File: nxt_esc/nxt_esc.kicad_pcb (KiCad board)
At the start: 2 copper layers, 47.6 x 47.6 mm, 18 parts, among them IC1 L293D, J1 NXT_MOTOR, J2 NXT_MOTOR, SW1 Skid Steer/Drive & Steer, SW2 Center Steering, U1 LM7805CT

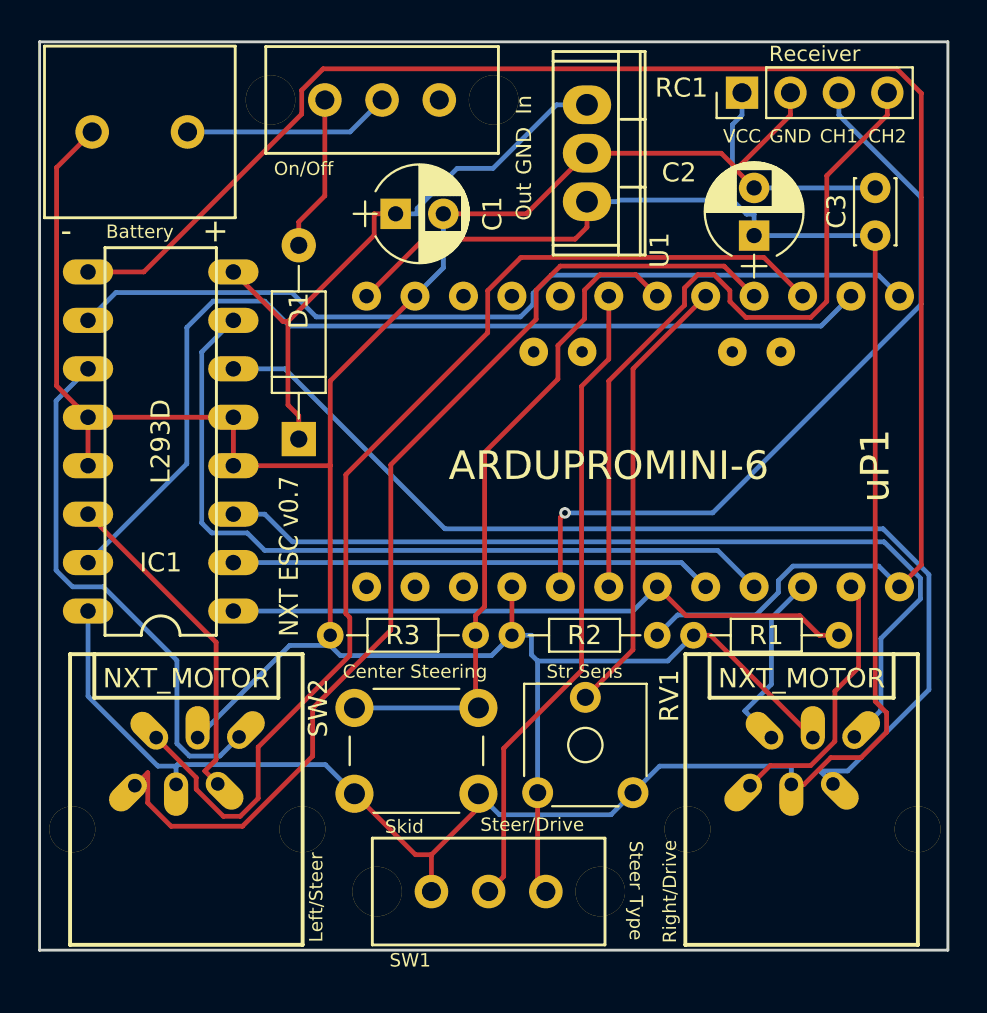
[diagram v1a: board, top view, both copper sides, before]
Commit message: Started adding wider traces
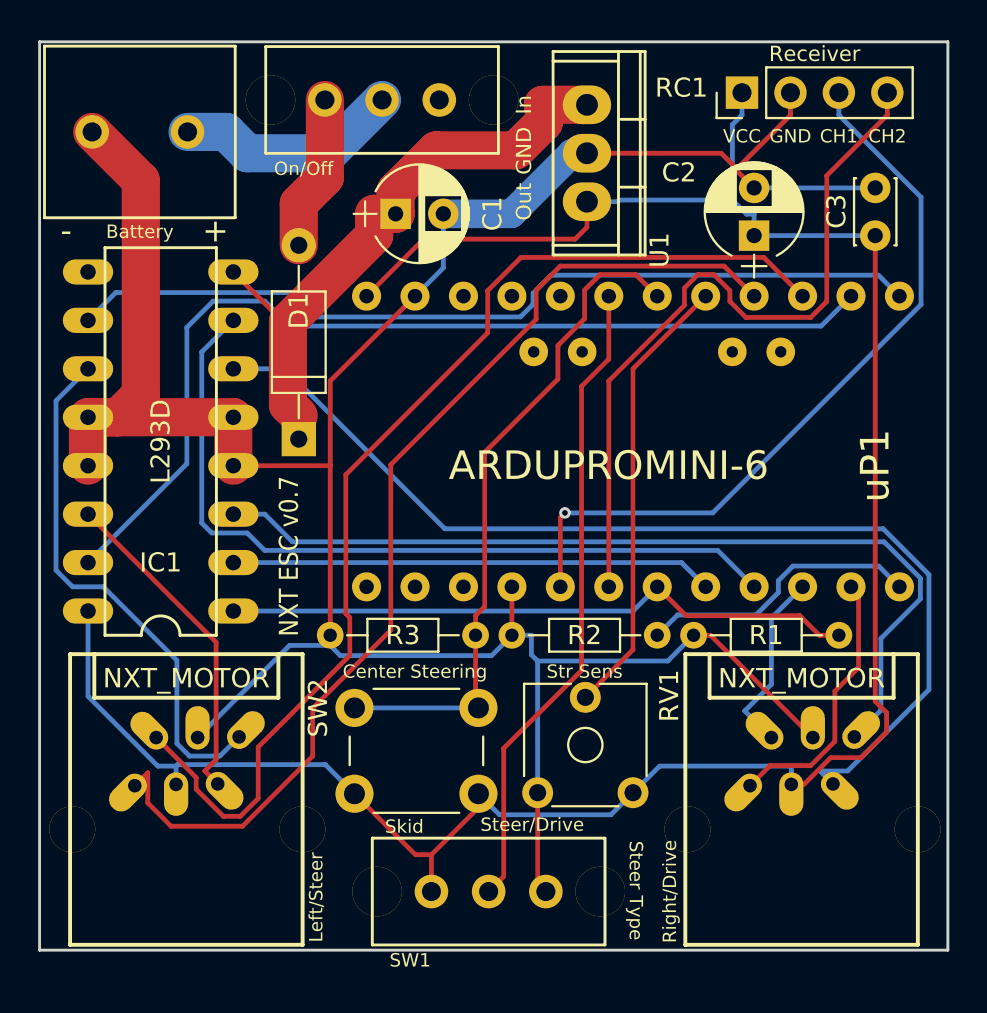
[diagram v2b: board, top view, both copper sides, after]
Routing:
- net Net-(IC1-Pad9): track 90.7 -> 15.0 mm
- net GND: track 142.9 -> 144.5 mm
- net VCC: track 31.5 -> 32.7 mm
- net Net-(BT1-Pad1): track 10.9 -> 11.8 mm
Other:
- net class H-Bridge Power added: clearance 0.2, trace_width 4, via_dia 4.5, via_drill 4.3
- net class Motor Power added: clearance 0.2, trace_width 1.5, via_dia 3, via_drill 2.8
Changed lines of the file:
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@@
   (general
     (links 57)
-    (no_connects 0)
-    (area 111.049999 65.73 176.91 125.170001)
+    (no_connects 1)
+    (area 111.049999 77.394999 158.825001 125.170001)
     (thickness 1.6)
     (drawings 24)
-    (tracks 254)
+    (tracks 251)
     (zones 0)
     (modules 18)
@@
   )
   (setup
-    (last_trace_width 0.25)
+    (last_trace_width 1.5)
     (user_trace_width 0.4)
+    (user_trace_width 0.75)
+    (user_trace_width 1.5)
     (trace_clearance 0.2)
     (zone_clearance 0.508)
@@
     (add_net "Net-(SW1-Pad2)")
     (add_net VCC)
+  )
+  (net_class "H-Bridge Power" ""
+    (clearance 0.2)
+    (trace_width 4)
+    (via_dia 4.5)
+    (via_drill 4.3)
+    (uvia_dia 2.3)
+    (uvia_drill 2)
+  )
+  (net_class "Motor Power" ""
+    (clearance 0.2)
+    (trace_width 1.5)
+    (via_dia 3)
+    (via_drill 2.8)
+    (uvia_dia 1.3)
+    (uvia_drill 0.8)
   )
   (module ArduProMiniTKB:ArduProMini-6 (layer F.Cu)
@@
   (segment (start 119.6273 93.7327) (end 119.6273 102.6983) (width 0.25) (layer B.Cu) (net 3))
   (segment (start 121.285 92.075) (end 119.6273 93.7327) (width 0.25) (layer B.Cu) (net 3))
-  (segment (start 139.827 80.772) (end 138.2317 80.772) (width 0.25) (layer B.Cu) (net 4))
-  (segment (start 129.794 86.487) (end 130.9193 86.487) (width 0.25) (layer B.Cu) (net 4))
-  (segment (start 134.8998 84.1039) (end 138.2317 80.772) (width 0.25) (layer B.Cu) (net 4))
-  (segment (start 133.021 84.1039) (end 134.8998 84.1039) (width 0.25) (layer B.Cu) (net 4))
-  (segment (start 130.9193 86.2056) (end 133.021 84.1039) (width 0.25) (layer B.Cu) (net 4))
-  (segment (start 130.9193 86.487) (end 130.9193 86.2056) (width 0.25) (layer B.Cu) (net 4))
+  (segment (start 139.827 80.772) (end 137.5156 80.772) (width 2) (layer F.Cu) (net 4) (status 400000))
+  (segment (start 129.794 85.2932) (end 129.794 86.487) (width 2) (layer F.Cu) (net 4) (status 800000))
+  (segment (start 131.9276 83.1596) (end 129.794 85.2932) (width 2) (layer F.Cu) (net 4))
+  (segment (start 136.0932 83.1596) (end 131.9276 83.1596) (width 2) (layer F.Cu) (net 4))
+  (segment (start 137.5664 81.6864) (end 136.0932 83.1596) (width 2) (layer F.Cu) (net 4))
+  (segment (start 137.5664 80.8228) (end 137.5664 81.6864) (width 2) (layer F.Cu) (net 4))
+  (segment (start 137.5156 80.772) (end 137.5664 80.8228) (width 2) (layer F.Cu) (net 4))
   (segment (start 123.883 92.133) (end 121.285 89.535) (width 0.25) (layer F.Cu) (net 4))
   (segment (start 124.148 92.133) (end 123.883 92.133) (width 0.25) (layer F.Cu) (net 4))
-  (segment (start 128.6687 87.6123) (end 124.148 92.133) (width 0.25) (layer F.Cu) (net 4))
-  (segment (start 128.6687 86.487) (end 128.6687 87.6123) (width 0.25) (layer F.Cu) (net 4))
-  (segment (start 124.148 96.5067) (end 124.714 97.0727) (width 0.25) (layer F.Cu) (net 4))
-  (segment (start 124.148 92.133) (end 124.148 96.5067) (width 0.25) (layer F.Cu) (net 4))
-  (segment (start 129.794 86.487) (end 128.6687 86.487) (width 0.25) (layer F.Cu) (net 4))
+  (segment (start 128.6687 87.6123) (end 124.148 92.133) (width 2) (layer F.Cu) (net 4))
+  (segment (start 128.6687 86.487) (end 128.6687 87.6123) (width 2) (layer F.Cu) (net 4))
+  (segment (start 124.148 96.5067) (end 124.714 97.0727) (width 2) (layer F.Cu) (net 4))
+  (segment (start 124.148 92.133) (end 124.148 96.5067) (width 2) (layer F.Cu) (net 4))
+  (segment (start 129.794 86.487) (end 128.6687 86.487) (width 2) (layer F.Cu) (net 4))
   (segment (start 124.714 98.298) (end 124.714 97.0727) (width 0.25) (layer F.Cu) (net 4))
   (segment (start 153.8425 113.9143) (end 155.24 112.5168) (width 0.25) (layer B.Cu) (net 5))
@@
   (segment (start 155.24 112.5168) (end 155.2399 112.5168) (width 0.25) (layer B.Cu) (net 5))
   (segment (start 121.285 102.235) (end 122.9311 102.235) (width 0.25) (layer B.Cu) (net 5))
+  (segment (start 132.294 86.487) (end 135.8646 86.487) (width 1.5) (layer B.Cu) (net 6) (status 400000))
+  (segment (start 135.8646 86.487) (end 139.0396 83.312) (width 1.5) (layer B.Cu) (net 6) (status 800000))
+  (segment (start 139.0396 83.312) (end 139.827 83.312) (width 1.5) (layer B.Cu) (net 6) (status C00000))
+  (segment (start 121.285 97.155) (end 121.285 99.695) (width 2) (layer F.Cu) (net 6))
+  (segment (start 113.665 97.155) (end 121.285 97.155) (width 2) (layer F.Cu) (net 6))
+  (segment (start 113.665 97.155) (end 113.665 99.695) (width 2) (layer F.Cu) (net 6))
+  (segment (start 113.665 97.155) (end 115.2398 97.155) (width 2) (layer F.Cu) (net 6))
+  (segment (start 116.4336 84.745) (end 113.883 82.1944) (width 2) (layer F.Cu) (net 6))
+  (segment (start 116.4336 95.9612) (end 116.4336 84.745) (width 2) (layer F.Cu) (net 6))
+  (segment (start 115.2398 97.155) (end 116.4336 95.9612) (width 2) (layer F.Cu) (net 6))
   (segment (start 154.94 85.13) (end 148.59 85.13) (width 0.25) (layer B.Cu) (net 6))
   (segment (start 135.89 108.585) (end 135.89 106.045) (width 0.25) (layer F.Cu) (net 6))
-  (segment (start 121.285 97.155) (end 121.285 99.695) (width 0.25) (layer F.Cu) (net 6))
-  (segment (start 113.665 97.155) (end 121.285 97.155) (width 0.25) (layer F.Cu) (net 6))
   (segment (start 150.495 80.137) (end 150.495 81.3123) (width 0.25) (layer F.Cu) (net 6))
   (segment (start 146.8667 83.312) (end 147.681 84.1263) (width 0.25) (layer F.Cu) (net 6))
@@
   (segment (start 124.2386 109.119) (end 119.4103 113.9473) (width 0.25) (layer B.Cu) (net 6))
   (segment (start 126.365 109.119) (end 124.2386 109.119) (width 0.25) (layer B.Cu) (net 6))
-  (segment (start 136.652 86.487) (end 139.827 83.312) (width 0.25) (layer F.Cu) (net 6))
-  (segment (start 132.294 86.487) (end 136.652 86.487) (width 0.25) (layer F.Cu) (net 6))
-  (segment (start 113.665 99.695) (end 113.665 97.155) (width 0.25) (layer F.Cu) (net 6))
-  (segment (start 112.0172 84.0602) (end 113.883 82.1944) (width 0.25) (layer F.Cu) (net 6))
-  (segment (start 112.0172 95.5072) (end 112.0172 84.0602) (width 0.25) (layer F.Cu) (net 6))
-  (segment (start 113.665 97.155) (end 112.0172 95.5072) (width 0.25) (layer F.Cu) (net 6))
   (segment (start 126.365 99.695) (end 121.285 99.695) (width 0.25) (layer F.Cu) (net 6))
   (segment (start 126.365 108.585) (end 126.365 99.695) (width 0.25) (layer F.Cu) (net 6))
@@
   (segment (start 153.4934 115.7017) (end 157.7586 111.4365) (width 0.25) (layer B.Cu) (net 7))
   (segment (start 152.0459 115.7017) (end 153.4934 115.7017) (width 0.25) (layer B.Cu) (net 7))
-  (segment (start 116.5906 89.535) (end 113.665 89.535) (width 0.25) (layer F.Cu) (net 8))
-  (segment (start 124.8676 81.258) (end 116.5906 89.535) (width 0.25) (layer F.Cu) (net 8))
-  (segment (start 124.8676 80.0081) (end 124.8676 81.258) (width 0.25) (layer F.Cu) (net 8))
-  (segment (start 125.9906 78.8851) (end 124.8676 80.0081) (width 0.25) (layer F.Cu) (net 8))
-  (segment (start 156.0751 78.8851) (end 125.9906 78.8851) (width 0.25) (layer F.Cu) (net 8))
-  (segment (start 157.3557 80.1657) (end 156.0751 78.8851) (width 0.25) (layer F.Cu) (net 8))
-  (segment (start 157.3557 104.8993) (end 157.3557 80.1657) (width 0.25) (layer F.Cu) (net 8))
-  (segment (start 156.21 106.045) (end 157.3557 104.8993) (width 0.25) (layer F.Cu) (net 8))
   (segment (start 155.1214 104.9564) (end 156.21 106.045) (width 0.25) (layer B.Cu) (net 8))
   (segment (start 150.6282 104.9564) (end 155.1214 104.9564) (width 0.25) (layer B.Cu) (net 8))
@@
   (segment (start 133.985 107.5597) (end 134.4609 107.0838) (width 0.25) (layer F.Cu) (net 22))
   (segment (start 133.985 108.585) (end 133.985 107.5597) (width 0.25) (layer F.Cu) (net 22))
-  (segment (start 127.4066 82.1944) (end 118.883 82.1944) (width 0.25) (layer B.Cu) (net 23))
-  (segment (start 129.083 80.518) (end 127.4066 82.1944) (width 0.25) (layer B.Cu) (net 23))
-  (segment (start 126.083 85.5437) (end 124.714 86.9127) (width 0.25) (layer F.Cu) (net 24))
-  (segment (start 126.083 80.518) (end 126.083 85.5437) (width 0.25) (layer F.Cu) (net 24))
-  (segment (start 124.714 88.138) (end 124.714 86.9127) (width 0.25) (layer F.Cu) (net 24))
+  (segment (start 118.883 82.1944) (end 120.904 82.1944) (width 2) (layer B.Cu) (net 23) (status 400000))
+  (segment (start 126.289 83.312) (end 129.083 80.518) (width 2) (layer B.Cu) (net 23) (status 800000))
+  (segment (start 122.0216 83.312) (end 126.289 83.312) (width 2) (layer B.Cu) (net 23))
+  (segment (start 120.904 82.1944) (end 122.0216 83.312) (width 2) (layer B.Cu) (net 23))
+  (segment (start 124.714 88.138) (end 124.714 85.9536) (width 2) (layer F.Cu) (net 24) (status 400000))
+  (segment (start 126.083 84.5846) (end 126.083 80.518) (width 2) (layer F.Cu) (net 24) (status 800000))
+  (segment (start 124.714 85.9536) (end 126.083 84.5846) (width 2) (layer F.Cu) (net 24))
 )
